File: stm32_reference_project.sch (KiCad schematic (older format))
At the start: 38 parts, among them J1 USB_Serial, J2 PROG_HDR, SW1 RESET, SW2 BOOT_SELECT, SW3 BAT_SELECT, U2 STM32F103C8Tx, Y1 8Mhz, Y2 32.768K

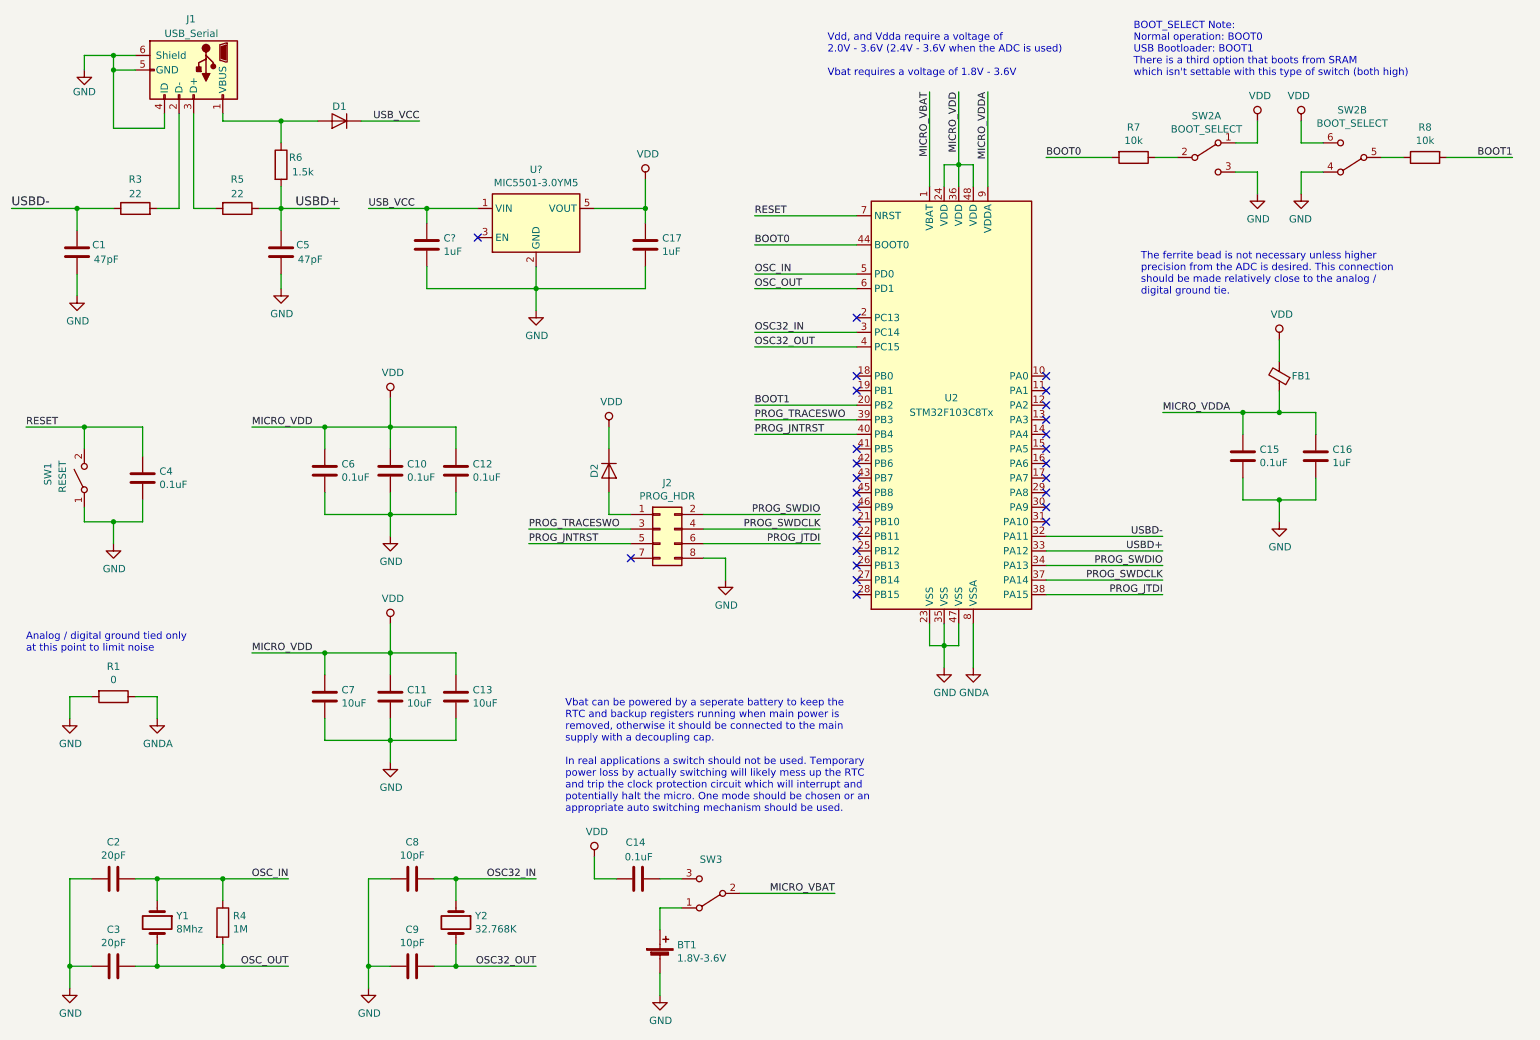
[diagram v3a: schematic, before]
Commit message: Refined the STM32 reference schematic
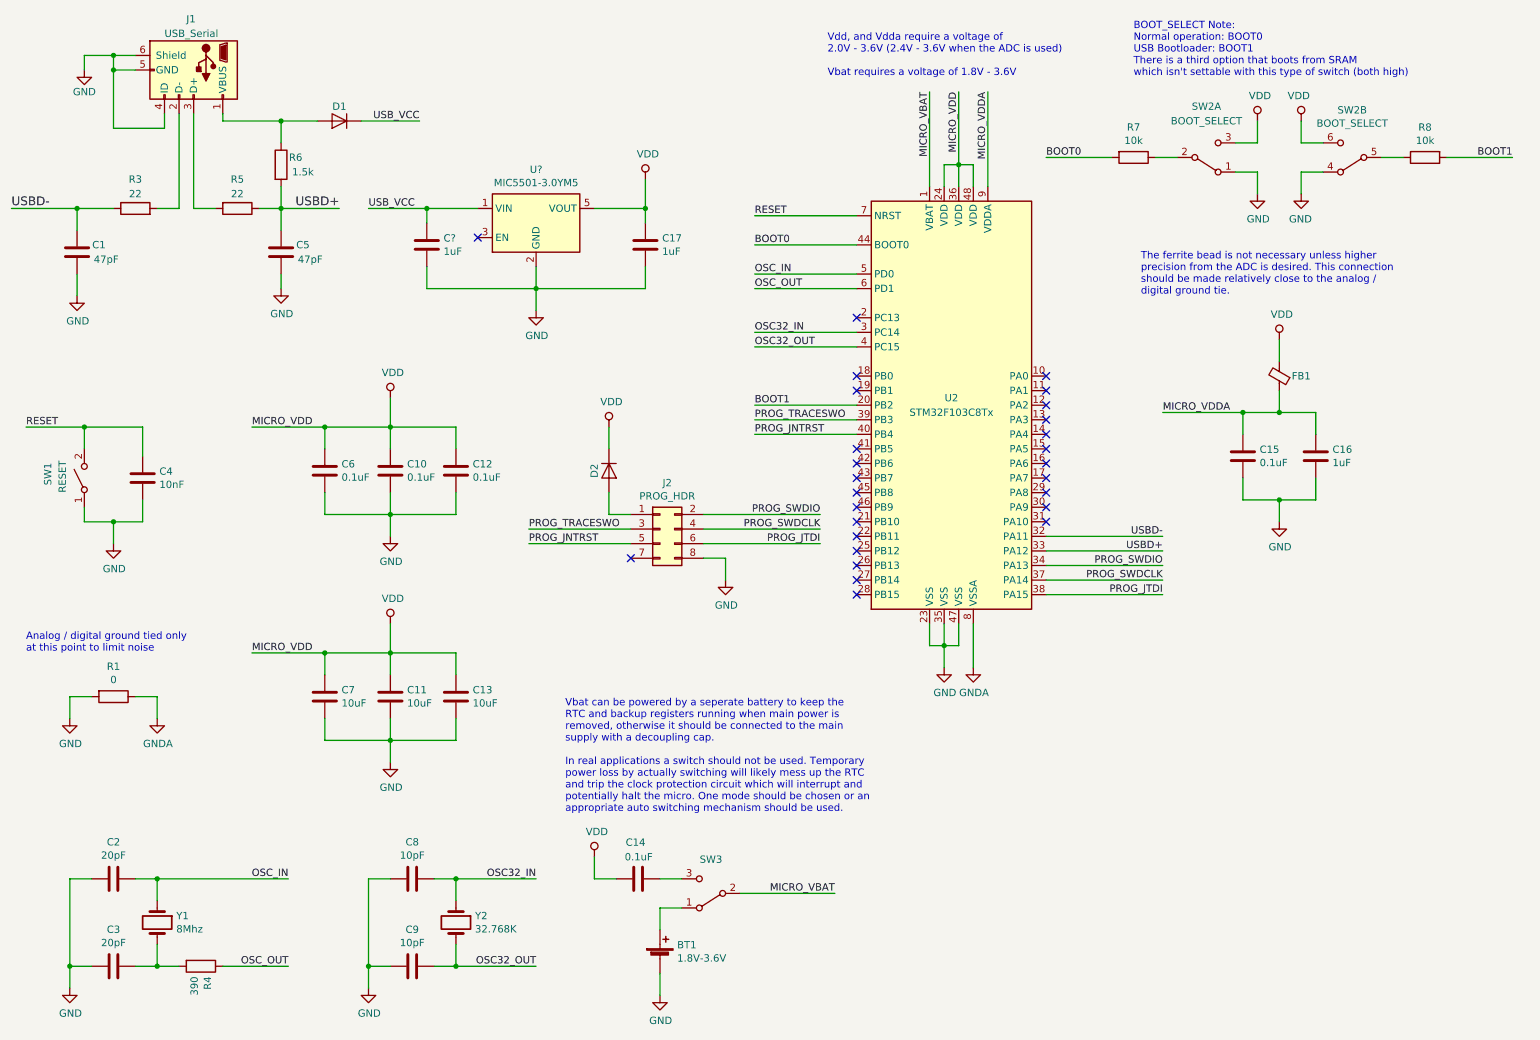
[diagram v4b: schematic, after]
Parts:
- C4: value 0.1uF -> 10nF
- R4: value 1M -> 390; Spice_Model 1Meg -> 390
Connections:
- net GND: now also SW2.1 (A); no longer SW2.3 (C)
- net OSC_IN: no longer R4.1
- net OSC_OUT: now also R4.1; no longer C3.1, R4.2, Y1.2
- net VDD: now also SW2.3 (C); no longer SW2.1 (A)
- new net: C3.1, R4.2, Y1.2
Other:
- moved on the sheet: R4
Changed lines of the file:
@@
-EESchema Schematic File Version 4
+EESchema Schematic File Version 5
 LIBS:stm32_reference_project-cache
 EELAYER 29 0
@@
 Wire Wire Line
 	1600 6500 1600 6650
-Connection ~ 1600 6500
-Connection ~ 1600 7100
 $Comp
 L Device:Crystal Y2
@@
 $EndComp
 $Comp
-L power:GND #PWR021
-U 1 1 5C194501
-P 9150 1800
-AR Path="/5C194501" Ref="#PWR021"  Part="1"
-AR Path="/5C77D6A4/5C194501" Ref="#PWR?"  Part="1"
-F 0 "#PWR021" H 9150 1550 50  0001 C CNN
-F 1 "GND" H 9155 1627 50  0000 C CNN
-F 2 "" H 9150 1800 50  0001 C CNN
-F 3 "" H 9150 1800 50  0001 C CNN
-	1    9150 1800
-	1    0    0    -1
-$EndComp
-$Comp
 L Device:R R7
 U 1 1 5C194511
@@
 U 1 1 5C541C87
 P 8800 1550
-F 0 "SW2" H 8800 1835 50  0000 C CNN
-F 1 "BOOT_SELECT" H 8800 1744 50  0000 C CNN
+F 0 "SW2" H 8800 1200 50  0000 C CNN
+F 1 "BOOT_SELECT" H 8800 1300 50  0000 C CNN
 F 2 "Button_Switch_THT:SW_E-Switch_EG1271_DPDT" H 8800 1550 50  0001 C CNN
 F 3 "" H 8800 1550 50  0001 C CNN
 	1    8800 1550
-	1    0    0    -1
+	1    0    0    1
 $EndComp
 Wire Wire Line
@@
 L Device:R R4
 U 1 1 5C5787B0
-P 2050 6800
-F 0 "R4" H 2120 6846 50  0000 L CNN
-F 1 "1M" H 2120 6755 50  0000 L CNN
-F 2 "Resistor_SMD:R_0603_1608Metric" V 1980 6800 50  0001 C CNN
-F 3 "" H 2050 6800 50  0001 C CNN
-F 4 "R" H 2050 6800 50  0001 C CNN "Spice_Primitive"
-F 5 "1Meg" H 2050 6800 50  0001 C CNN "Spice_Model"
-F 6 "Y" H 2050 6800 50  0001 C CNN "Spice_Netlist_Enabled"
-	1    2050 6800
-	1    0    0    -1
-$EndComp
-Wire Wire Line
-	1600 6500 2050 6500
-Wire Wire Line
-	1600 7100 2050 7100
-Wire Wire Line
-	2050 6950 2050 7100
-Wire Wire Line
-	2050 6650 2050 6500
-Wire Wire Line
-	2500 7100 2050 7100
-Connection ~ 2050 7100
-Wire Wire Line
-	2500 6500 2050 6500
-Connection ~ 2050 6500
+P 1900 7100
+F 0 "R4" H 1970 7146 50  0000 L CNN
+F 1 "390" H 1970 7055 50  0000 L CNN
+F 2 "Resistor_SMD:R_0603_1608Metric" V 1830 7100 50  0001 C CNN
+F 3 "" H 1900 7100 50  0001 C CNN
+F 4 "R" H 1900 7100 50  0001 C CNN "Spice_Primitive"
+F 5 "390" H 1900 7100 50  0001 C CNN "Spice_Model"
+F 6 "Y" H 1900 7100 50  0001 C CNN "Spice_Netlist_Enabled"
+	1    1900 7100
+	0    1    1    0
+$EndComp
 Wire Wire Line
 	3200 3400 3200 3200
@@
 Wire Wire Line
 	9300 2800 9300 2950
-$Comp
-L power:VDD #PWR020
-U 1 1 5C964291
-P 9150 1300
-F 0 "#PWR020" H 9150 1150 50  0001 C CNN
-F 1 "VDD" H 9167 1473 50  0000 C CNN
-F 2 "" H 9150 1300 50  0001 C CNN
-F 3 "" H 9150 1300 50  0001 C CNN
-	1    9150 1300
-	1    0    0    -1
-$EndComp
 $Comp
 L power:VDD #PWR022
@@
 P 1500 3750
 F 0 "C4" H 1615 3796 50  0000 L CNN
-F 1 "0.1uF" H 1615 3705 50  0000 L CNN
+F 1 "10nF" H 1615 3705 50  0000 L CNN
 F 2 "" H 1538 3600 50  0001 C CNN
 F 3 "" H 1500 3750 50  0001 C CNN
@@
 	1    0    0    -1
 $EndComp
+$Comp
+L power:VDD #PWR020
+U 1 1 5C964291
+P 9150 1300
+F 0 "#PWR020" H 9150 1150 50  0001 C CNN
+F 1 "VDD" H 9167 1473 50  0000 C CNN
+F 2 "" H 9150 1300 50  0001 C CNN
+F 3 "" H 9150 1300 50  0001 C CNN
+	1    9150 1300
+	1    0    0    -1
+$EndComp
+$Comp
+L power:GND #PWR021
+U 1 1 5C194501
+P 9150 1800
+AR Path="/5C194501" Ref="#PWR021"  Part="1"
+AR Path="/5C77D6A4/5C194501" Ref="#PWR?"  Part="1"
+F 0 "#PWR021" H 9150 1550 50  0001 C CNN
+F 1 "GND" H 9155 1627 50  0000 C CNN
+F 2 "" H 9150 1800 50  0001 C CNN
+F 3 "" H 9150 1800 50  0001 C CNN
+	1    9150 1800
+	1    0    0    -1
+$EndComp
+Wire Wire Line
+	1600 7100 1750 7100
+Connection ~ 1600 7100
+Wire Wire Line
+	2050 7100 2500 7100
+Wire Wire Line
+	2500 6500 1600 6500
+Connection ~ 1600 6500
 $EndSCHEMATC

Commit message: Add the LEDs back to the circuit
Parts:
- added D3, D4: LED, symbol Device:LED
- added R7, R8: 390, symbol Device:R
- gave numbers to parts that had none: 2
- renumbered C8 to C10, C9 to C11, C12 to C13, C13 to C14, C14 to C15, C17 to C16, C15 to C17, C16 to C18, C10 to C8, C11 to C9, R3 to R2, R4 to R3, R5 to R4, R6 to R5, R7 to R6, R8 to R9, SW3 to SW2, SW2 to SW3
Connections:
- net labels added: PROG_LED
- wire segments 168 -> 178
- no-connect marks 27 -> 26
